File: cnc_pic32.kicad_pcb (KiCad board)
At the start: 2 copper layers, 96 x 96 mm, 132 parts, among them J1 icd, J10 tp, J11 tp, J12 tp, J13 FT232RL, J15 pololu, J16 pololu, J17 pololu, J18 pololu, J19 pololu, J2 USB_B_Mini, J20 pololu, J21 conector oled ST1306 128x32, J22 USB_B_Mini, J23 mrf24j40_tp, J24 mrf24j40_tp, J25 Conn_01x08_Pin, J3 tp, J4 tp, J5 tp, J6 tp, J7 tp, J8 tp, J9 tp, Q1 FDN306P, Q2 2N7002, Q3 2N7002, SW1 power, SW2 up, SW3 down, SW4 left, SW5 rigth, U1 PIC32MX795F512L-80x-PF, U2 LM1117DT-3.3, U3 FT232BM, U4 93CxxA, U5 MRF24J40MA, U6 LM1117DT-3.3, Y1 8MHZ, Y2 Crystal

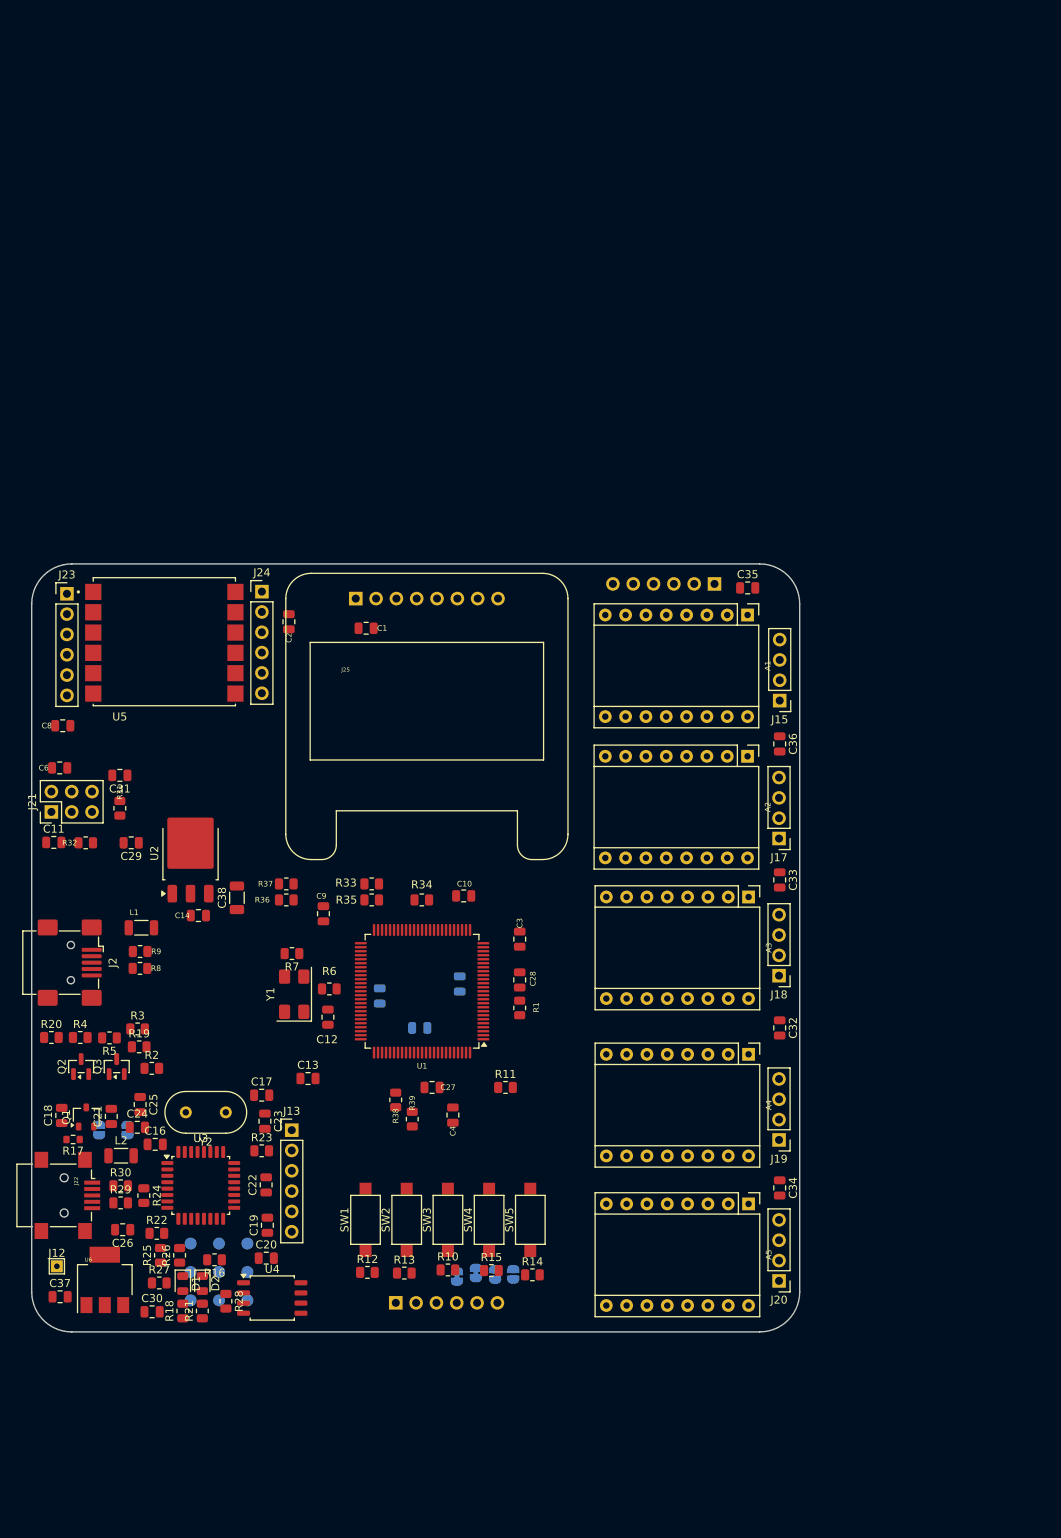
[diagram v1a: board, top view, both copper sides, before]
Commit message: feat: add MA240011 module sheet with labeled pins + Altium socket footprint
Esquemático
- Nueva hoja hija MA240011.kicad_sch (módulo PIC32 TQFP-100) referenciada
  desde la hoja MA240011 de mcu.kicad_sch
- mcu.kicad_sch: los 83 pines jerárquicos de MA240011 quedan rotulados con un
  label local del mismo nombre; 81 de ellos con un tramo de wire de 2.54 mm
  (un label solo no conecta a un pin de hoja) y RD4/RD5 sobre el wire existente
- mcu.kicad_sch: borde derecho del sheet 104.775 -> 106.68 mm y sus 41 pines,
  para quedar en grilla de 1.27 mm (evita 41 avisos endpoint_off_grid)
- ERC: 341 -> 158 violaciones; pin_not_connected 120 -> 39,
  isolated_pin_label 113 -> 10, endpoint_off_grid 6 -> 6
- power / zigbee / oled / pololu / cnc_pic32: pines MS1-MS3, conectores y
  anotacion de netnames

PCB
- Referencia de los 132 footprints a size 0.8 x 0.8 mm y thickness 0.12 mm
  (render_cache obsoleto eliminado para forzar el re-render)

Footprints
- lib/altium.pretty/MA240011_Socket_TQFP100_100pin.kicad_mod: zocalo adaptador
  de 100 pines TH pitch 1.27 mm convertido desde altium/Multimedia/MM20141127.PcbDoc
  (J4, patron MA240011); pads girados 90 grados sentido horario
- fp-lib-table: alta de la biblioteca "altium" (${KIPRJMOD}/lib/altium.pretty)

.gitignore
- Ignorar altium/, tmp/ y *.bkp (backups de KiCad)
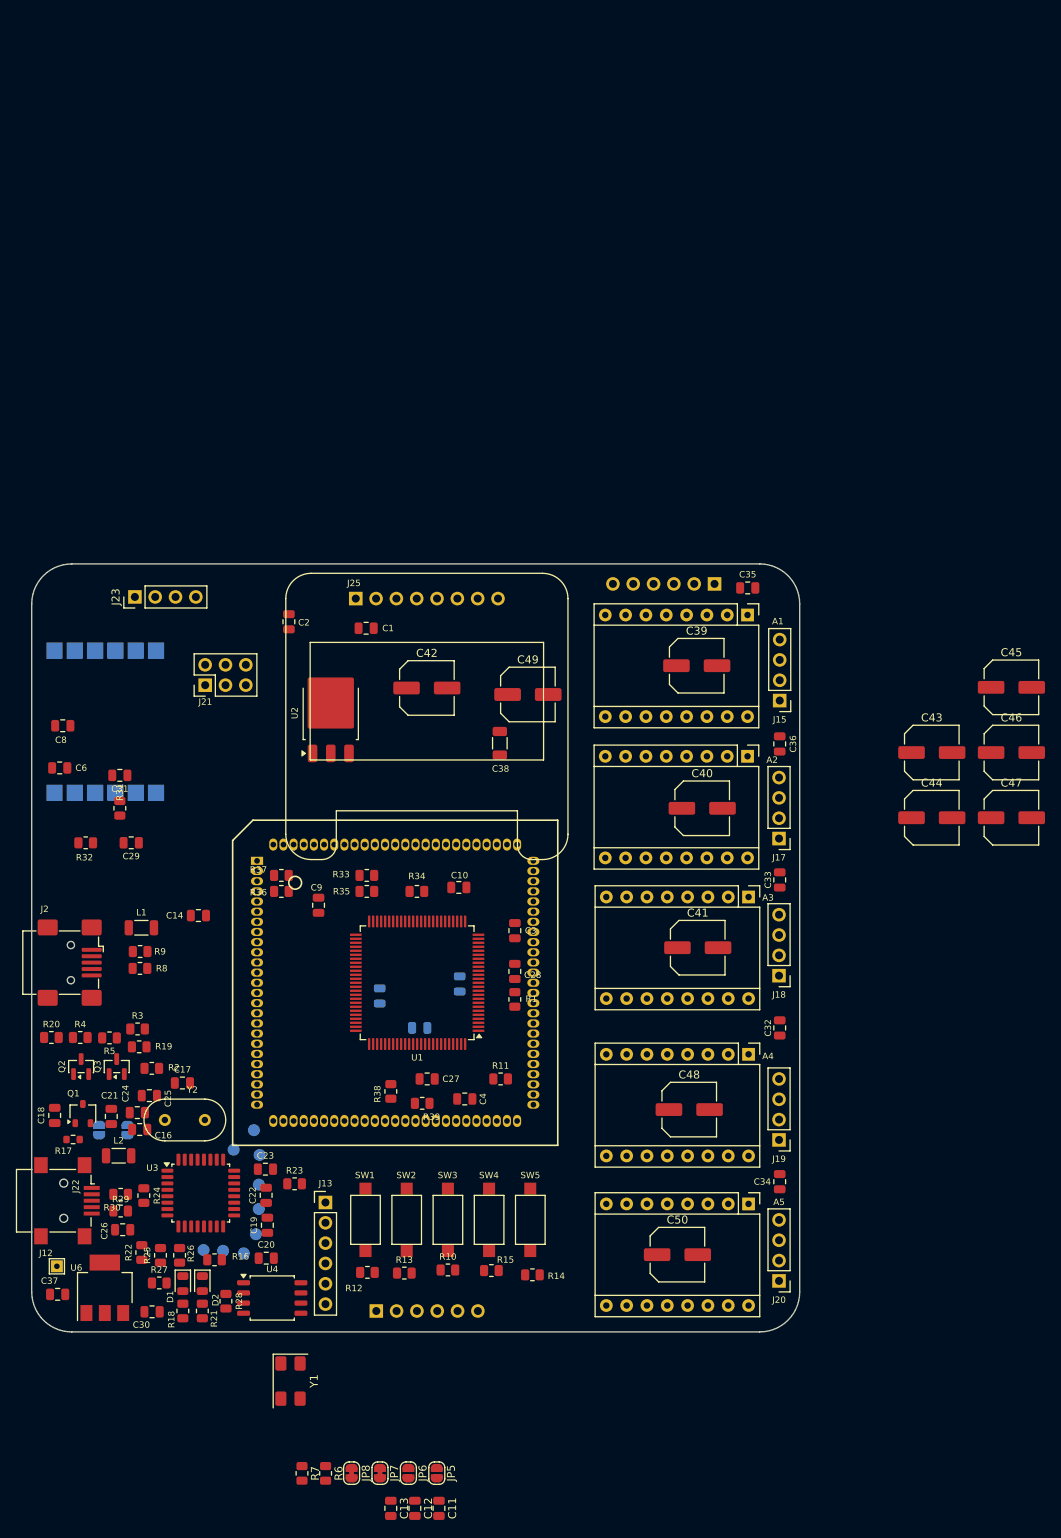
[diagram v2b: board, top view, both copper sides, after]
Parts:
- removed J24: mrf24j40_tp, Connector_PinHeader_2.54mm:PinHeader_1x06_P2.54mm_Vertical
- added C39: 10uf, Capacitor_SMD:C_Elec_6.3x5.4, F.Cu at (135.1, 38.7)
- added C40: 10uf, Capacitor_SMD:C_Elec_6.3x5.4, F.Cu at (135.8, 56.5)
- added C41: 10uf, Capacitor_SMD:C_Elec_6.3x5.4, F.Cu at (135.3, 74.0)
- added C42: 10uf, Capacitor_SMD:C_Elec_6.3x5.4, F.Cu at (101.4, 41.5)
- added C43: 10uf, Capacitor_SMD:C_Elec_6.3x5.4, F.Cu at (164.5, 49.6)
- added C44: 10uf, Capacitor_SMD:C_Elec_6.3x5.4, F.Cu at (164.5, 57.7)
- added C45: 10uf, Capacitor_SMD:C_Elec_6.3x5.4, F.Cu at (174.5, 41.4)
- added C46: 10uf, Capacitor_SMD:C_Elec_6.3x5.4, F.Cu at (174.5, 49.6)
- added C47: 10uf, Capacitor_SMD:C_Elec_6.3x5.4, F.Cu at (174.5, 57.7)
- added C48: 10uf, Capacitor_SMD:C_Elec_6.3x5.4, F.Cu at (134.2, 94.2)
- added C49: 10uf, Capacitor_SMD:C_Elec_6.3x5.4, F.Cu at (114.0, 42.3)
- added C50: 10uf, Capacitor_SMD:C_Elec_6.3x5.4, F.Cu at (132.7, 112.3)
- added U7: PIC32MX795F512L-80x-PF, altium:MA240011_Socket_TQFP100_100pin, F.Cu at (80.2, 63.1)
- J23: value mrf24j40_tp -> Conn_01x04_Pin; footprint Connector_PinHeader_2.54mm:PinHeader_1x06_P2.54mm_Vertical -> Connector_PinHeader_2.54mm:PinHeader_1x04_P2.54mm_Vertical
- JP5, JP6, JP7, JP8: moved to F.Cu
- U5: moved to B.Cu
- moved C11 96.2 mm to (102.9, 144.1), turned to -90 degrees
- moved R7 65.0 mm to (85.8, 139.7), turned to -90 degrees
- moved C12 62.4 mm to (99.9, 144.1)
- moved R6 60.6 mm to (88.7, 139.7), turned to -90 degrees
- moved C13 54.7 mm to (96.9, 144.1), turned to -90 degrees
- moved Y1 48.4 mm to (84.3, 128.1), turned to -90 degrees
- moved C38 38.1 mm to (110.5, 48.4)
- moved JP6 28.1 mm to (99.1, 139.7)
- moved JP8 27.9 mm to (92.0, 139.7), turned to -90 degrees
- moved JP7 27.7 mm to (95.5, 139.7), turned to -90 degrees
- moved JP5 25.9 mm to (102.6, 139.7)
- moved J21 24.9 mm to (73.7, 41.2)
- moved U2 24.8 mm to (89.4, 44.6)
- moved J5 18.9 mm to (77.2, 99.2)
- moved J9 16.2 mm to (79.8, 96.8)
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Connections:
- net /zigbee/CS_mrf renamed /MCU/RF3
- net /zigbee/MISO_mrf renamed /MCU/RF2
- A1 pad 10: unconnected-(A1-MS1-Pad10) -> /M1
- A1 pad 11: unconnected-(A1-MS2-Pad11) -> /M2
- A1 pad 12: unconnected-(A1-MS3-Pad12) -> /M3
- A2 pad 10: unconnected-(A2-MS1-Pad10) -> /M1
- A2 pad 11: unconnected-(A2-MS2-Pad11) -> /M2
- A2 pad 12: unconnected-(A2-MS3-Pad12) -> /M3
- A3 pad 10: unconnected-(A3-MS1-Pad10) -> /M1
- A3 pad 11: unconnected-(A3-MS2-Pad11) -> /M2
- A3 pad 12: unconnected-(A3-MS3-Pad12) -> /M3
- A4 pad 10: unconnected-(A4-MS1-Pad10) -> /M1
- A4 pad 11: unconnected-(A4-MS2-Pad11) -> /M2
- A4 pad 12: unconnected-(A4-MS3-Pad12) -> /M3
- A4 pad 16: unconnected-(A4-DIR-Pad16) -> /MCU/RE5
- A5 pad 10: unconnected-(A5-MS1-Pad10) -> /M1
- A5 pad 11: unconnected-(A5-MS2-Pad11) -> /M2
- A5 pad 12: unconnected-(A5-MS3-Pad12) -> /M3
- C13 pad 1: /MCU/OSC1 -> /MCU/MA240011/OSC1
- J23 pad 2: /zigbee/reset_mrf -> +3.3V
- J23 pad 3: /zigbee/wake_mrf -> /Oled/SCL
- J23 pad 4: /zigbee/INT_mrf -> /Oled/SDA
- J25 pad 3: /Oled/SCK -> /MCU/RG0
- J25 pad 4: /Oled/DIN -> /MCU/RG1
- J25 pad 5: /Oled/RES -> /MCU/RG6
- J25 pad 6: /Oled/DC -> /MCU/RG7
- J25 pad 7: /Oled/CS -> /MCU/RG8
- J25 pad 8: /Oled/BLK -> /MCU/RG9
- R33 pad 2: /zigbee/reset_mrf -> /MCU/RF4
- R34 pad 2: /zigbee/INT_mrf -> /MCU/RF12
- R35 pad 1: /zigbee/wake_mrf -> /MCU/RF5
- R38 pad 2: /zigbee/SCK_mrf -> /MCU/RF1
- R39 pad 2: /zigbee/MOSI_mrf -> /MCU/RF0
- R6 pad 1: /MCU/OSC2 -> /MCU/MA240011/OSC2
- R7 pad 2: /MCU/OSC1 -> /MCU/MA240011/OSC1
- U1 pad 40: /zigbee/INT_mrf -> /MCU/RF12
- U1 pad 49: /zigbee/reset_mrf -> /MCU/RF4
- U1 pad 50: /zigbee/wake_mrf -> /MCU/RF5
- U1 pad 53: /MCU/RF8 -> /M3
- U1 pad 66: /MCU/RA14 -> /M1
- U1 pad 67: /MCU/RA15 -> /M2
- U1 pad 84: /MCU/RD7 -> /RD7
- U1 pad 87: /zigbee/MOSI_mrf -> /MCU/RF0
- U1 pad 88: /zigbee/SCK_mrf -> /MCU/RF1
- U5 pad 2: /zigbee/reset_mrf -> /MCU/RF4
- U5 pad 3: /zigbee/wake_mrf -> /MCU/RF5
- U5 pad 4: /zigbee/INT_mrf -> /MCU/RF12
- U5 pad 5: /zigbee/MOSI_mrf -> /MCU/RF0
- U5 pad 6: /zigbee/SCK_mrf -> /MCU/RF1
- Y1 pad 3: /MCU/OSC1 -> /MCU/MA240011/OSC1

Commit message: add files
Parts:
- removed JP5: pgc1, Jumper:SolderJumper-2_P1.3mm_Open_RoundedPad1.0x1.5mm
- removed JP6: pgd1, Jumper:SolderJumper-2_P1.3mm_Open_RoundedPad1.0x1.5mm
- removed JP7: pgc2, Jumper:SolderJumper-2_P1.3mm_Bridged_RoundedPad1.0x1.5mm
- removed JP8: pgd2, Jumper:SolderJumper-2_P1.3mm_Bridged_RoundedPad1.0x1.5mm
- removed U5: MRF24J40MA, Library:MODULE_MRF24J40MA
- added D3: LED, Diode_SMD:D_0805_2012Metric, F.Cu at (70.8, 48.4)
- added D4: LED, Diode_SMD:D_0805_2012Metric, F.Cu at (65.9, 48.7)
- added D5: LED, Diode_SMD:D_0805_2012Metric, F.Cu at (68.3, 48.8)
- added JP10: MS2, Jumper:SolderJumper-2_P1.3mm_Open_RoundedPad1.0x1.5mm, B.Cu at (128.8, 41.8)
- added JP11: MS3, Jumper:SolderJumper-2_P1.3mm_Open_RoundedPad1.0x1.5mm, B.Cu at (132.3, 41.8)
- added JP12: MS1, Jumper:SolderJumper-2_P1.3mm_Open_RoundedPad1.0x1.5mm, B.Cu at (125.2, 77.1)
- added JP13: MS2, Jumper:SolderJumper-2_P1.3mm_Open_RoundedPad1.0x1.5mm, B.Cu at (128.8, 77.1)
- added JP14: MS3, Jumper:SolderJumper-2_P1.3mm_Open_RoundedPad1.0x1.5mm, B.Cu at (132.3, 77.1)
- added JP15: MS1, Jumper:SolderJumper-2_P1.3mm_Open_RoundedPad1.0x1.5mm, B.Cu at (125.0, 59.6)
- added JP16: MS2, Jumper:SolderJumper-2_P1.3mm_Open_RoundedPad1.0x1.5mm, B.Cu at (128.5, 59.6)
- added JP17: MS3, Jumper:SolderJumper-2_P1.3mm_Open_RoundedPad1.0x1.5mm, B.Cu at (132.1, 59.6)
- added JP18: MS1, Jumper:SolderJumper-2_P1.3mm_Open_RoundedPad1.0x1.5mm, B.Cu at (124.9, 96.7)
- added JP19: MS2, Jumper:SolderJumper-2_P1.3mm_Open_RoundedPad1.0x1.5mm, B.Cu at (128.5, 96.7)
- added JP20: MS3, Jumper:SolderJumper-2_P1.3mm_Open_RoundedPad1.0x1.5mm, B.Cu at (132.0, 96.7)
- added JP21: MS1, Jumper:SolderJumper-2_P1.3mm_Open_RoundedPad1.0x1.5mm, B.Cu at (125.2, 115.8)
- added JP22: MS2, Jumper:SolderJumper-2_P1.3mm_Open_RoundedPad1.0x1.5mm, B.Cu at (128.7, 115.8)
- added JP23: MS3, Jumper:SolderJumper-2_P1.3mm_Open_RoundedPad1.0x1.5mm, B.Cu at (132.3, 115.8)
- added JP3: sda_jp, Jumper:SolderJumper-2_P1.3mm_Open_RoundedPad1.0x1.5mm, F.Cu at (76.8, 85.1)
- added JP4: scl_jp, Jumper:SolderJumper-2_P1.3mm_Open_RoundedPad1.0x1.5mm, F.Cu at (76.8, 88.6)
- added JP9: MS1, Jumper:SolderJumper-2_P1.3mm_Open_RoundedPad1.0x1.5mm, B.Cu at (125.2, 41.8)
- added R40: 1k, Resistor_SMD:R_0805_2012Metric, F.Cu at (66.1, 52.3)
- added R41: 1k, Resistor_SMD:R_0805_2012Metric, F.Cu at (68.5, 52.4)
- added R42: 0, Resistor_SMD:R_0805_2012Metric, F.Cu at (77.1, 67.5)
- added R43: 0, Resistor_SMD:R_0805_2012Metric, F.Cu at (77.1, 64.7)
- added U8: ESP8266-12E_ESP-12E, RF_Module:ESP-12E, F.Cu at (66.0, 31.9)
- C14, C15: value 100nf -> 4.7uf
- L1: footprint Inductor_SMD:L_1206_3216Metric -> Inductor_SMD:L_1210_3225Metric
- R35: value 2k2 -> 1k
- U4: moved to B.Cu
- moved C12 69.7 mm to (87.9, 75.4), turned to 0 degrees
- moved R7 64.7 mm to (84.9, 75.0)
- moved R6 59.3 mm to (89.8, 80.4), turned to 90 degrees
- moved C13 58.9 mm to (88.0, 85.8), turned to 180 degrees
- moved U7 47.8 mm to (116.8, 93.9), turned to 180 degrees
- moved Y1 47.7 mm to (86.2, 80.4)
- moved J23 32.0 mm to (96.6, 34.0)
- moved C11 27.8 mm to (98.8, 116.5), turned to 0 degrees
- moved R35 27.5 mm to (70.8, 52.1), turned to -90 degrees
- moved U4 16.3 mm to (69.3, 107.6), turned to 180 degrees
- moved C31 12.4 mm to (72.7, 60.2)
- moved C8 8.62 mm to (55.9, 54.8)
- moved C6 6.24 mm to (55.5, 57.7)
- moved J21 6.22 mm to (79.7, 39.6)
- moved R36 5.56 mm to (86.2, 71.6)
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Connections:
- net /Ft232/FT_USB_BM renamed /Ft232/FT_USB_DM
- net /MCU/RD14 renamed /U4RX
- net /MCU/RD15 renamed /U4TX
- A1 pad 10: /M1 -> Net-(A1-MS1)
- A1 pad 11: /M2 -> Net-(A1-MS2)
- A1 pad 12: /M3 -> Net-(A1-MS3)
- A2 pad 10: /M1 -> Net-(A2-MS1)
- A2 pad 11: /M2 -> Net-(A2-MS2)
- A2 pad 12: /M3 -> Net-(A2-MS3)
- A3 pad 10: /M1 -> Net-(A3-MS1)
- A3 pad 11: /M2 -> Net-(A3-MS2)
- A3 pad 12: /M3 -> Net-(A3-MS3)
- A3 pad 7: unconnected-(A3-GND-Pad7) -> GND
- A4 pad 10: /M1 -> Net-(A4-MS1)
- A4 pad 11: /M2 -> Net-(A4-MS2)
- A4 pad 12: /M3 -> Net-(A4-MS3)
- A5 pad 10: /M1 -> Net-(A5-MS1)
- A5 pad 11: /M2 -> Net-(A5-MS2)
- A5 pad 12: /M3 -> Net-(A5-MS3)
- C16 pad 2: GND1 -> GND
- C17 pad 2: GND1 -> GND
- C19 pad 1: GND1 -> GND
- C20 pad 1: GND1 -> GND
- C24 pad 2: GND1 -> GND
- C26 pad 2: GND1 -> GND
- J2 pad 6: GND -> unconnected-(J2-Shield-Pad6)_1
- J21 pad 3: /Oled/SDA -> /MCU/RA15
- J21 pad 5: /Oled/SCL -> /MCU/RA14
- J22 pad 5: GND -> Net-(J22-GND1)
- J23 pad 3: /Oled/SCL -> /MCU/RA14
- J23 pad 4: /Oled/SDA -> /MCU/RA15
- J25 pad 3: /MCU/RG0 -> /MCU/RG6
- J25 pad 4: /MCU/RG1 -> /MCU/RG8
- J25 pad 5: /MCU/RG6 -> /MCU/RG12
- J25 pad 6: /MCU/RG7 -> /MCU/RG13
- J25 pad 7: /MCU/RG8 -> /MCU/RG14
- J25 pad 8: /MCU/RG9 -> /MCU/RG15
- R31 pad 2: /Oled/SCL -> /MCU/RA14
- R32 pad 2: /Oled/SDA -> /MCU/RA15
- R35 pad 1: /MCU/RF5 -> Net-(D3-K)
- U1 pad 53: /M3 -> /MCU/RF8
- U1 pad 54: /MCU/VBUS -> Net-(U1-VBUS)
- U1 pad 66: /M1 -> /MCU/RA14
- U1 pad 67: /M2 -> /MCU/RA15
- U1 pad 72: /MCU/RD0 -> /M1
- U1 pad 76: /MCU/RD1 -> /M2
- U1 pad 85: +3.3V -> /MCU/VCAP_VDD_CORE
- U1 pad 90: /MCU/RG0 -> /M3
- U7 pad 53: /M3 -> /MCU/RF8
- U7 pad 54: /MCU/VBUS -> Net-(U7-VBUS)
- U7 pad 66: /M1 -> /MCU/RA14
- U7 pad 67: /M2 -> /MCU/RA15
- U7 pad 90: /MCU/RG0 -> /M3
